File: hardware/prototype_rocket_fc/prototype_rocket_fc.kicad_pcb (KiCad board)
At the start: 2 copper layers, 100 x 60 mm, 25 parts, among them J1 BATTERY_IN, U1 SD_Card_Reader, U2 Teensy4.0, U3 GY-BMP280, U4 TinyGPS++, U5 MPU9250_custom, U6 LMR50410XFDBVR, U7 MIC5504-3.3YM5

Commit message: RFD version of pcb files
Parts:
- added U8: RFD900x_Mech, myFootprints:RFD900x_Mech, B.Cu at (109.2, 53.8)
- added U9: RFD900x_Pins, myFootprints:RFD900x_Pins, F.Cu at (109.1, 42.7)
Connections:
- U2 pad 10: Net-(U2-Pad10) -> /TX2
- U2 pad 9: Net-(U2-Pad9) -> /RX2
- U4 pad 2: /RX1 -> /RX2
- U4 pad 3: /TX1 -> /TX2
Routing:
- net /RX2: track 0.00 -> 50.2 mm
- net /TX2: track 0.00 -> 47.2 mm
- net /RX1: track 68.0 -> 81.2 mm
- net /TX1: track 64.6 -> 72.9 mm
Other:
- board text added: "1"
- board text added: "RFD900x"

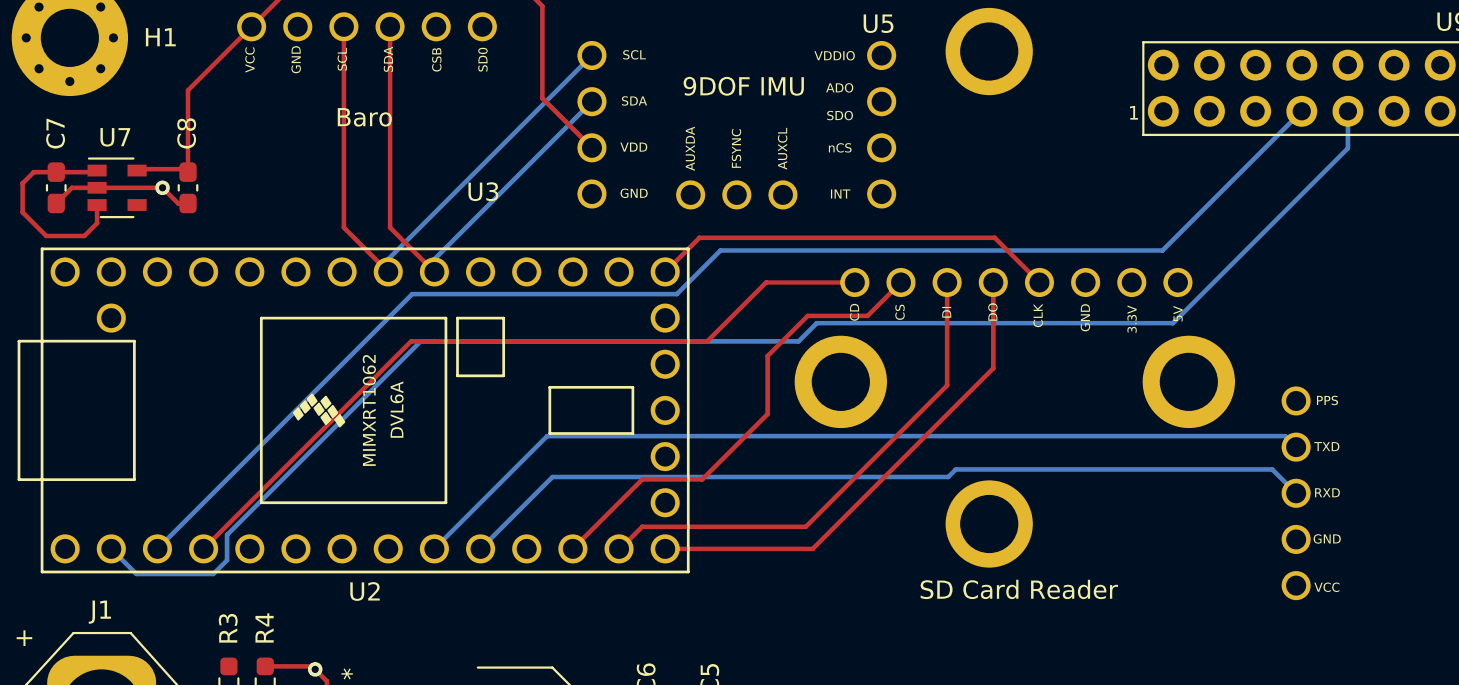
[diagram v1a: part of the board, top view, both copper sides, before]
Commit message: Fixing ground not connected
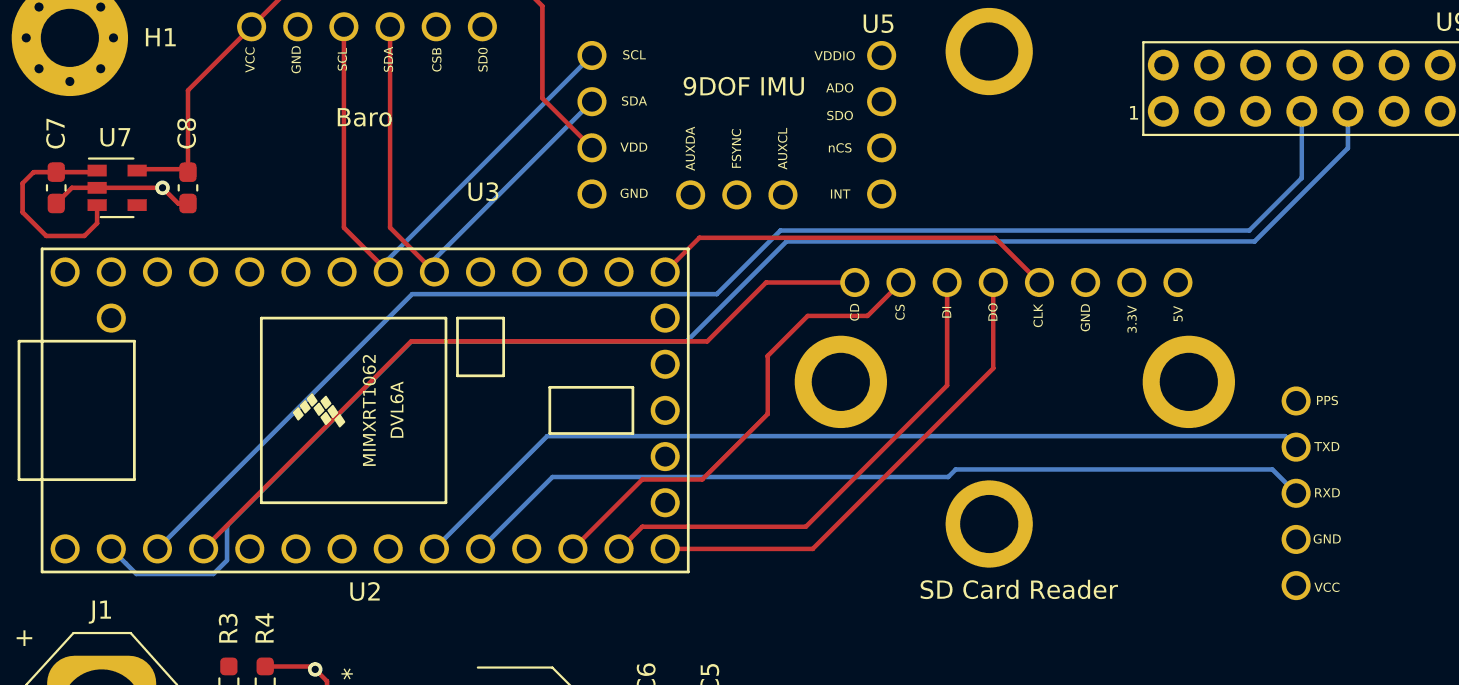
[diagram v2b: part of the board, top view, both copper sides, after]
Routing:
- net /TX1: track 72.9 -> 75.1 mm
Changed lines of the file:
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@@
-(kicad_pcb (version 20171130) (host pcbnew 5.1.10-88a1d61d58~88~ubuntu18.04.1)
+(kicad_pcb (version 20171130) (host pcbnew 5.0.2+dfsg1-1)
   (general
     (thickness 1.6)
     (drawings 18)
-    (tracks 120)
+    (tracks 122)
     (zones 0)
     (modules 27)
@@
     (zone_45_only no)
     (trace_min 0.2)
+    (segment_width 0.2)
+    (edge_width 0.05)
     (via_size 0.8)
     (via_drill 0.4)
@@
     (uvia_min_size 0.2)
     (uvia_min_drill 0.1)
-    (edge_width 0.05)
-    (segment_width 0.2)
     (pcb_text_width 0.3)
     (pcb_text_size 1.5 1.5)
@@
     (pad_drill 0.762)
     (pad_to_mask_clearance 0)
+    (solder_mask_min_width 0.25)
     (aux_axis_origin 0 0)
     (visible_elements FFFFFF7F)
@@
   (segment (start 55.08 50.44) (end 57.52 52.88) (width 0.25) (layer F.Cu) (net 24))
   (segment (start 55.08 39.39) (end 55.08 50.44) (width 0.25) (layer F.Cu) (net 24))
-  (segment (start 73.4 54.1) (end 58.84 54.1) (width 0.25) (layer B.Cu) (net 36))
+  (segment (start 79.1 50.6) (end 75.6 54.1) (width 0.25) (layer B.Cu) (net 36))
+  (segment (start 104.9 50.6) (end 79.1 50.6) (width 0.25) (layer B.Cu) (net 36))
   (segment (start 58.84 54.1) (end 44.82 68.12) (width 0.25) (layer B.Cu) (net 36))
-  (segment (start 75.8 51.7) (end 73.4 54.1) (width 0.25) (layer B.Cu) (net 36))
-  (segment (start 107.79 44.04) (end 100.13 51.7) (width 0.25) (layer B.Cu) (net 36))
-  (segment (start 100.13 51.7) (end 75.8 51.7) (width 0.25) (layer B.Cu) (net 36))
-  (segment (start 43.66 69.5) (end 42.28 68.12) (width 0.25) (layer B.Cu) (net 37))
+  (segment (start 75.6 54.1) (end 58.84 54.1) (width 0.25) (layer B.Cu) (net 36))
+  (segment (start 107.79 44.04) (end 107.79 47.71) (width 0.25) (layer B.Cu) (net 36))
+  (segment (start 107.79 47.71) (end 104.9 50.6) (width 0.25) (layer B.Cu) (net 36))
+  (segment (start 43.66 69.5) (end 43.079999 68.919999) (width 0.25) (layer B.Cu) (net 37))
   (segment (start 47.9 69.5) (end 43.66 69.5) (width 0.25) (layer B.Cu) (net 37))
+  (segment (start 43.079999 68.919999) (end 42.28 68.12) (width 0.25) (layer B.Cu) (net 37))
   (segment (start 48.65 68.75) (end 47.9 69.5) (width 0.25) (layer B.Cu) (net 37))
-  (segment (start 48.65 67.35) (end 48.65 68.75) (width 0.25) (layer B.Cu) (net 37))
+  (segment (start 48.65 66.85) (end 48.65 68.75) (width 0.25) (layer B.Cu) (net 37))
   (segment (start 110.33 44.04) (end 110.33 46.07) (width 0.25) (layer B.Cu) (net 37))
-  (segment (start 81.1 55.7) (end 80.1 56.7) (width 0.25) (layer B.Cu) (net 37))
-  (segment (start 110.33 46.07) (end 100.7 55.7) (width 0.25) (layer B.Cu) (net 37))
-  (segment (start 80.1 56.7) (end 59.3 56.7) (width 0.25) (layer B.Cu) (net 37))
-  (segment (start 100.7 55.7) (end 81.1 55.7) (width 0.25) (layer B.Cu) (net 37))
-  (segment (start 59.3 56.7) (end 48.65 67.35) (width 0.25) (layer B.Cu) (net 37))
+  (segment (start 110.33 46.07) (end 105.2 51.2) (width 0.25) (layer B.Cu) (net 37))
+  (segment (start 79.43641 51.2) (end 73.93641 56.7) (width 0.25) (layer B.Cu) (net 37))
+  (segment (start 73.93641 56.7) (end 58.8 56.7) (width 0.25) (layer B.Cu) (net 37))
+  (segment (start 105.2 51.2) (end 79.43641 51.2) (width 0.25) (layer B.Cu) (net 37))
+  (segment (start 58.8 56.7) (end 48.65 66.85) (width 0.25) (layer B.Cu) (net 37))
   (segment (start 74.8925 86.1675) (end 74.9 86.175) (width 0.25) (layer F.Cu) (net 51))
   (segment (start 72.35 86.1675) (end 74.8925 86.1675) (width 0.25) (layer F.Cu) (net 51))
